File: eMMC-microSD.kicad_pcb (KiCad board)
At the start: 4 copper layers, 15 x 17.6 mm, 45 parts, among them J1 Micro_SD_Card, J2 Micro_SD_Card, J3 Micro_SD_Card, J4 Micro_SD_Card, J5 Micro_SD_Card, U1 eMMC_5.1_BGA153, U2 eMMC_5.1_BGA153, U3 eMMC_5.1_BGA153, U4 eMMC_5.1_BGA153, U5 eMMC_5.1_BGA153

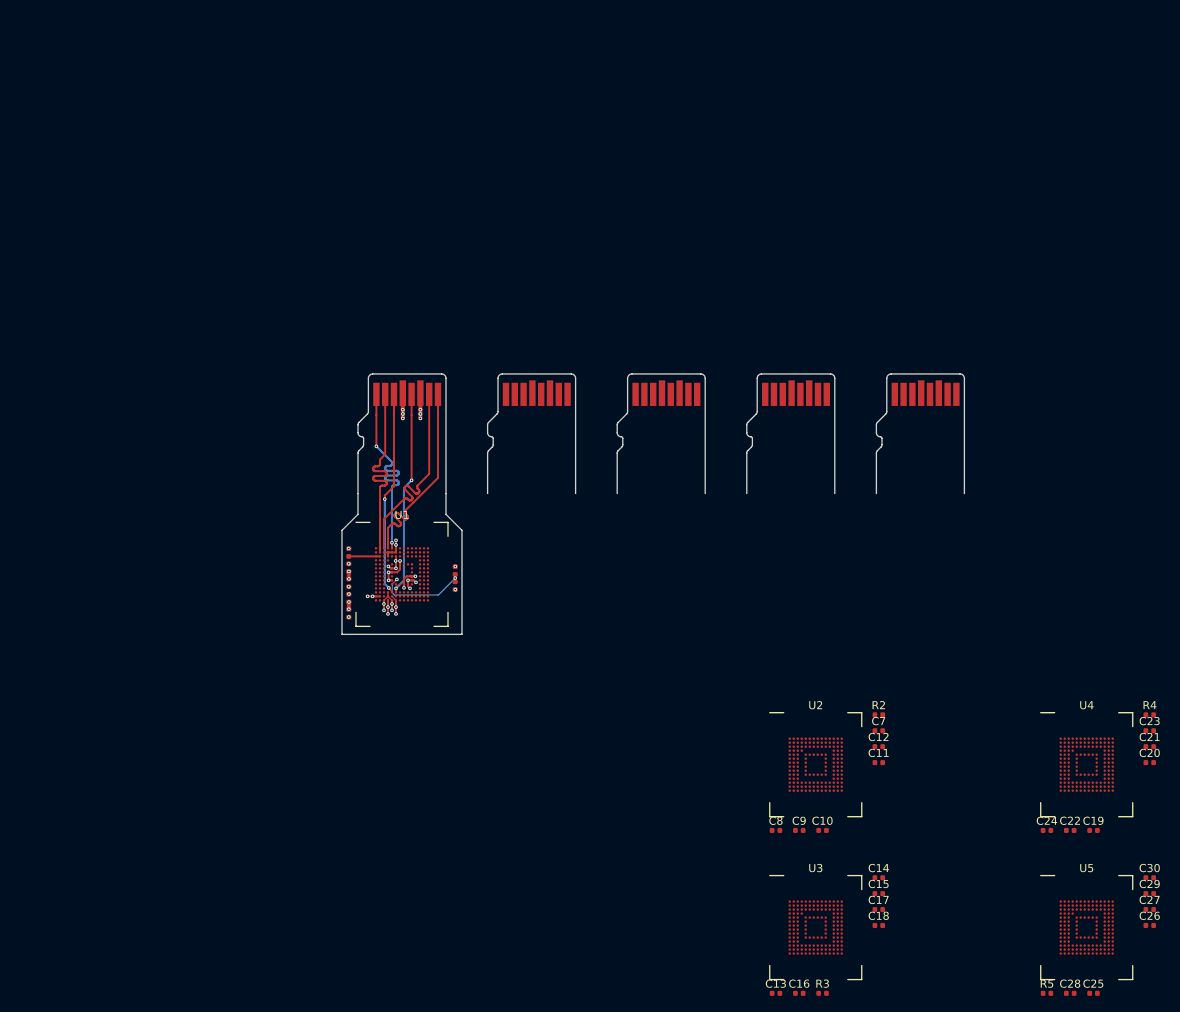
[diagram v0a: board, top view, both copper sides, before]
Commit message: Panelize
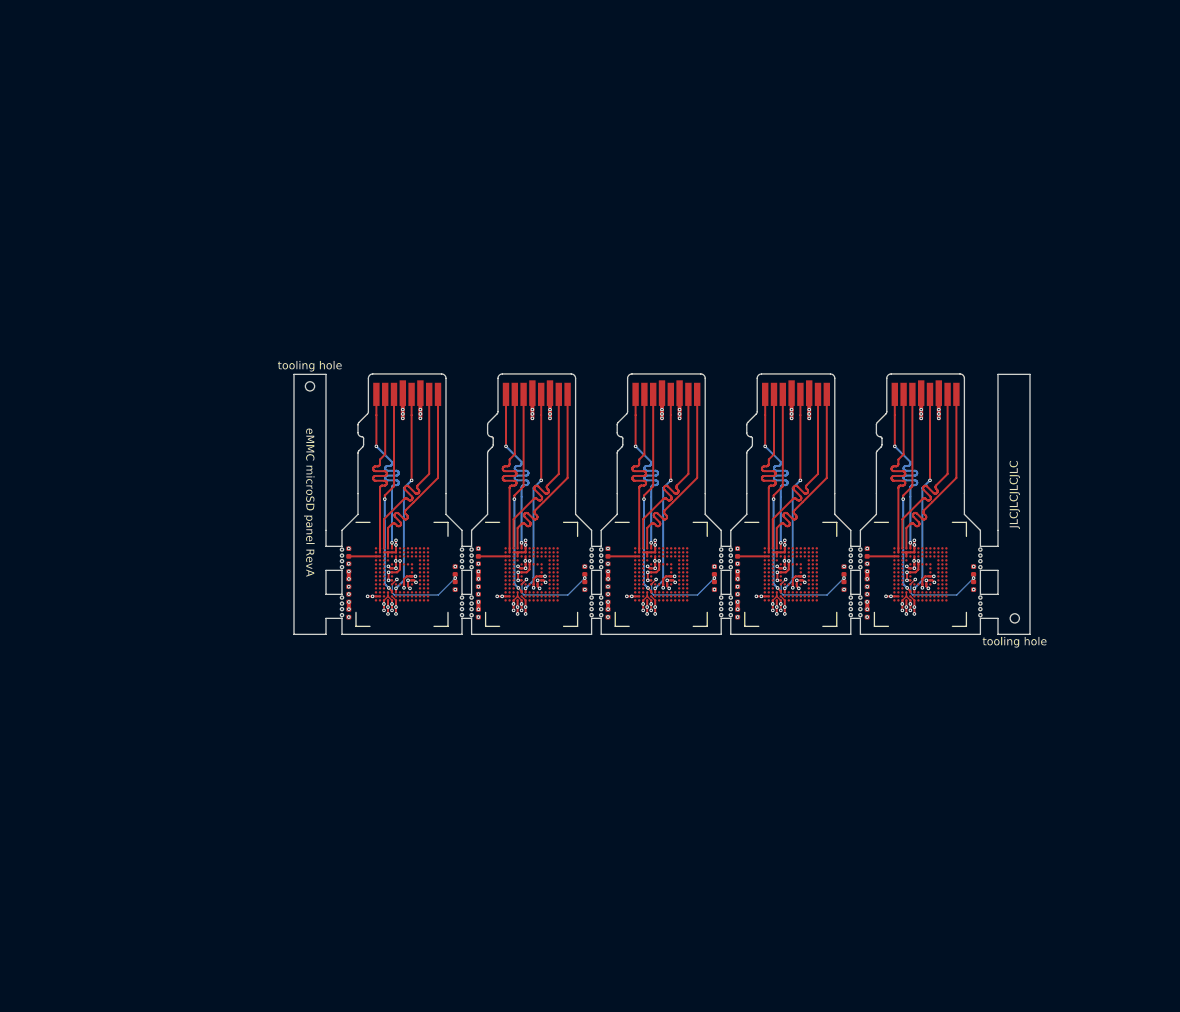
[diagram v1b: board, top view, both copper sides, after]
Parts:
- added REF**: ToolingHole_JLCSMT, ToolingHole:ToolingHole_JLCSMT, F.Cu at (171.1, 143.0)
- added REF**: Perforation_0.4mm, Perforation:Perforation_0.4mm, F.Cu at (166.8, 141.8)
- added REF**: Perforation_0.4mm, Perforation:Perforation_0.4mm, F.Cu at (87.0, 141.8)
- added REF**: Perforation_0.4mm, Perforation:Perforation_0.4mm, F.Cu at (87.0, 135.2)
- added REF**: Perforation_0.4mm, Perforation:Perforation_0.4mm, F.Cu at (87.0, 141.2)
- added REF**: Perforation_0.4mm, Perforation:Perforation_0.4mm, F.Cu at (87.0, 135.8)
- added REF**: Perforation_0.4mm, Perforation:Perforation_0.4mm, F.Cu at (87.0, 142.6)
- added REF**: Perforation_0.4mm, Perforation:Perforation_0.4mm, F.Cu at (87.0, 140.4)
- added REF**: Perforation_0.4mm, Perforation:Perforation_0.4mm, F.Cu at (87.0, 136.6)
- added REF**: Perforation_0.4mm, Perforation:Perforation_0.4mm, F.Cu at (87.0, 134.4)
- added REF**: Perforation_0.4mm, Perforation:Perforation_0.4mm, F.Cu at (151.8, 141.8)
- added REF**: ToolingHole_JLCSMT, ToolingHole:ToolingHole_JLCSMT, F.Cu at (83.0, 114.0)
- added REF**: Perforation_0.4mm, Perforation:Perforation_0.4mm, F.Cu at (150.6, 141.2)
- added REF**: Perforation_0.4mm, Perforation:Perforation_0.4mm, F.Cu at (150.6, 141.8)
- added REF**: Perforation_0.4mm, Perforation:Perforation_0.4mm, F.Cu at (150.6, 134.4)
- added REF**: Perforation_0.4mm, Perforation:Perforation_0.4mm, F.Cu at (150.6, 140.4)
- added REF**: Perforation_0.4mm, Perforation:Perforation_0.4mm, F.Cu at (151.8, 135.2)
- added REF**: Perforation_0.4mm, Perforation:Perforation_0.4mm, F.Cu at (151.8, 141.2)
- added REF**: Perforation_0.4mm, Perforation:Perforation_0.4mm, F.Cu at (151.8, 135.8)
- added REF**: Perforation_0.4mm, Perforation:Perforation_0.4mm, F.Cu at (151.8, 142.6)
- added REF**: Perforation_0.4mm, Perforation:Perforation_0.4mm, F.Cu at (151.8, 140.4)
- added REF**: Perforation_0.4mm, Perforation:Perforation_0.4mm, F.Cu at (151.8, 136.6)
- added REF**: Perforation_0.4mm, Perforation:Perforation_0.4mm, F.Cu at (166.8, 134.4)
- added REF**: Perforation_0.4mm, Perforation:Perforation_0.4mm, F.Cu at (151.8, 134.4)
- added REF**: Perforation_0.4mm, Perforation:Perforation_0.4mm, F.Cu at (150.6, 136.6)
- added REF**: Perforation_0.4mm, Perforation:Perforation_0.4mm, F.Cu at (150.6, 142.6)
- added REF**: Perforation_0.4mm, Perforation:Perforation_0.4mm, F.Cu at (150.6, 135.2)
- added REF**: Perforation_0.4mm, Perforation:Perforation_0.4mm, F.Cu at (150.6, 135.8)
- added REF**: Perforation_0.4mm, Perforation:Perforation_0.4mm, F.Cu at (135.6, 141.8)
- added REF**: Perforation_0.4mm, Perforation:Perforation_0.4mm, F.Cu at (134.4, 141.2)
- added REF**: Perforation_0.4mm, Perforation:Perforation_0.4mm, F.Cu at (134.4, 141.8)
- added REF**: Perforation_0.4mm, Perforation:Perforation_0.4mm, F.Cu at (134.4, 134.4)
- added REF**: Perforation_0.4mm, Perforation:Perforation_0.4mm, F.Cu at (134.4, 140.4)
- added REF**: Perforation_0.4mm, Perforation:Perforation_0.4mm, F.Cu at (166.8, 142.6)
- added REF**: Perforation_0.4mm, Perforation:Perforation_0.4mm, F.Cu at (135.6, 135.2)
- added REF**: Perforation_0.4mm, Perforation:Perforation_0.4mm, F.Cu at (135.6, 141.2)
- added REF**: Perforation_0.4mm, Perforation:Perforation_0.4mm, F.Cu at (135.6, 135.8)
- added REF**: Perforation_0.4mm, Perforation:Perforation_0.4mm, F.Cu at (135.6, 142.6)
- added REF**: Perforation_0.4mm, Perforation:Perforation_0.4mm, F.Cu at (135.6, 140.4)
- added REF**: Perforation_0.4mm, Perforation:Perforation_0.4mm, F.Cu at (135.6, 136.6)
- added REF**: Perforation_0.4mm, Perforation:Perforation_0.4mm, F.Cu at (135.6, 134.4)
- added REF**: Perforation_0.4mm, Perforation:Perforation_0.4mm, F.Cu at (134.4, 136.6)
- added REF**: Perforation_0.4mm, Perforation:Perforation_0.4mm, F.Cu at (134.4, 142.6)
- added REF**: Perforation_0.4mm, Perforation:Perforation_0.4mm, F.Cu at (134.4, 135.2)
- added REF**: Perforation_0.4mm, Perforation:Perforation_0.4mm, F.Cu at (166.8, 141.2)
- added REF**: Perforation_0.4mm, Perforation:Perforation_0.4mm, F.Cu at (134.4, 135.8)
- added REF**: Perforation_0.4mm, Perforation:Perforation_0.4mm, F.Cu at (119.4, 141.8)
- added REF**: Perforation_0.4mm, Perforation:Perforation_0.4mm, F.Cu at (118.2, 141.2)
- added REF**: Perforation_0.4mm, Perforation:Perforation_0.4mm, F.Cu at (118.2, 141.8)
- added REF**: Perforation_0.4mm, Perforation:Perforation_0.4mm, F.Cu at (118.2, 134.4)
- added REF**: Perforation_0.4mm, Perforation:Perforation_0.4mm, F.Cu at (118.2, 140.4)
- added REF**: Perforation_0.4mm, Perforation:Perforation_0.4mm, F.Cu at (119.4, 135.2)
- added REF**: Perforation_0.4mm, Perforation:Perforation_0.4mm, F.Cu at (119.4, 141.2)
- added REF**: Perforation_0.4mm, Perforation:Perforation_0.4mm, F.Cu at (119.4, 135.8)
- added REF**: Perforation_0.4mm, Perforation:Perforation_0.4mm, F.Cu at (119.4, 142.6)
- added REF**: Perforation_0.4mm, Perforation:Perforation_0.4mm, F.Cu at (166.8, 135.2)
- added REF**: Perforation_0.4mm, Perforation:Perforation_0.4mm, F.Cu at (119.4, 140.4)
- added REF**: Perforation_0.4mm, Perforation:Perforation_0.4mm, F.Cu at (119.4, 136.6)
- added REF**: Perforation_0.4mm, Perforation:Perforation_0.4mm, F.Cu at (119.4, 134.4)
- added REF**: Perforation_0.4mm, Perforation:Perforation_0.4mm, F.Cu at (118.2, 136.6)
- added REF**: Perforation_0.4mm, Perforation:Perforation_0.4mm, F.Cu at (118.2, 142.6)
- added REF**: Perforation_0.4mm, Perforation:Perforation_0.4mm, F.Cu at (118.2, 135.2)
- added REF**: Perforation_0.4mm, Perforation:Perforation_0.4mm, F.Cu at (118.2, 135.8)
- added REF**: Perforation_0.4mm, Perforation:Perforation_0.4mm, F.Cu at (103.2, 140.4)
- added REF**: Perforation_0.4mm, Perforation:Perforation_0.4mm, F.Cu at (103.2, 142.6)
- added REF**: Perforation_0.4mm, Perforation:Perforation_0.4mm, F.Cu at (103.2, 141.2)
- added REF**: Perforation_0.4mm, Perforation:Perforation_0.4mm, F.Cu at (166.8, 135.8)
- added REF**: Perforation_0.4mm, Perforation:Perforation_0.4mm, F.Cu at (103.2, 141.8)
- added REF**: Perforation_0.4mm, Perforation:Perforation_0.4mm, F.Cu at (102.0, 140.4)
- added REF**: Perforation_0.4mm, Perforation:Perforation_0.4mm, F.Cu at (102.0, 142.6)
- added REF**: Perforation_0.4mm, Perforation:Perforation_0.4mm, F.Cu at (102.0, 141.2)
- added REF**: Perforation_0.4mm, Perforation:Perforation_0.4mm, F.Cu at (102.0, 141.8)
- added REF**: Perforation_0.4mm, Perforation:Perforation_0.4mm, F.Cu at (103.2, 134.4)
- added REF**: Perforation_0.4mm, Perforation:Perforation_0.4mm, F.Cu at (103.2, 136.6)
- added REF**: Perforation_0.4mm, Perforation:Perforation_0.4mm, F.Cu at (103.2, 135.2)
- added REF**: Perforation_0.4mm, Perforation:Perforation_0.4mm, F.Cu at (103.2, 135.8)
- added REF**: Perforation_0.4mm, Perforation:Perforation_0.4mm, F.Cu at (102.0, 135.2)
- added REF**: Perforation_0.4mm, Perforation:Perforation_0.4mm, F.Cu at (166.8, 136.6)
- added REF**: Perforation_0.4mm, Perforation:Perforation_0.4mm, F.Cu at (102.0, 135.8)
- added REF**: Perforation_0.4mm, Perforation:Perforation_0.4mm, F.Cu at (102.0, 136.6)
- added REF**: Perforation_0.4mm, Perforation:Perforation_0.4mm, F.Cu at (102.0, 134.4)
- added REF**: Perforation_0.4mm, Perforation:Perforation_0.4mm, F.Cu at (166.8, 140.4)
- moved C26 58.5 mm to (152.7, 134.8), turned to 90 degrees
- moved C20 57.8 mm to (136.4, 134.8), turned to 90 degrees
- moved C28 57.2 mm to (152.7, 138.6), turned to 270 degrees
- moved C16 56.6 mm to (120.2, 138.6), turned to 270 degrees
- moved C18 56.1 mm to (120.2, 136.7), turned to 90 degrees
- moved C25 54.9 mm to (165.9, 137.0), turned to 270 degrees
- moved C12 54.8 mm to (104.0, 136.7), turned to 90 degrees
- moved C21 54.8 mm to (136.4, 140.5), turned to 90 degrees
- moved C23 53.6 mm to (136.4, 142.4), turned to 270 degrees
- moved C11 53.4 mm to (104.0, 142.4), turned to 270 degrees
- moved C13 53.4 mm to (133.6, 137.0), turned to 270 degrees
- moved C10 53.0 mm to (104.0, 138.6), turned to 270 degrees
- moved C14 52.9 mm to (120.2, 134.8), turned to 90 degrees
- moved R3 52.7 mm to (133.6, 138.9), turned to 90 degrees
- moved C27 52.6 mm to (152.7, 140.5), turned to 90 degrees
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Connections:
- U1 pad A2: (no net) -> /Adapter 1/DAT3
- U2 pad A2: (no net) -> /Adapter 2/DAT3
- U3 pad A2: (no net) -> /Adapter 3/DAT3
- U4 pad A2: (no net) -> /Adapter 4/DAT3
- U5 pad A2: (no net) -> /Adapter 5/DAT3
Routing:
- net GND: track 19.2 -> 96.1 mm, vias 22 -> 110
- net VCC: track 14.1 -> 70.4 mm, vias 18 -> 90
- net /Adapter 3/DAT3: track 0.00 -> 25.6 mm
- net /Adapter 4/DAT3: track 0.00 -> 25.6 mm
- net /Adapter 2/DAT3: track 0.00 -> 25.6 mm
- net /Sheet5F2931E6/DAT3: track 25.6 -> 0.00 mm
- net /Adapter 1/DAT3: track 0.00 -> 25.6 mm
- net /Adapter 5/DAT3: track 0.00 -> 25.6 mm
- net /Adapter 5/DAT2: track 0.00 -> 25.6 mm, vias 0 -> 2
- net /Adapter 4/DAT2: track 0.00 -> 25.6 mm, vias 0 -> 2
- net /Adapter 2/DAT2: track 0.00 -> 25.6 mm, vias 0 -> 2
- net /Adapter 3/DAT2: track 0.00 -> 25.6 mm, vias 0 -> 2
- net /Adapter 2/DAT1: track 0.00 -> 25.6 mm
- net /Adapter 5/DAT1: track 0.00 -> 25.6 mm
- net /Adapter 4/DAT1: track 0.00 -> 25.6 mm
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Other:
- board size 15 x 17.6 mm -> 92 x 32.5 mm
- board text added: "JLCJLCJLCJLC"
- board text added: "eMMC micro SD Rev A Tobias Schramm 2020"
- board text added: "eMMC microSD panel RevA"

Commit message: Redo termination and layout of first module
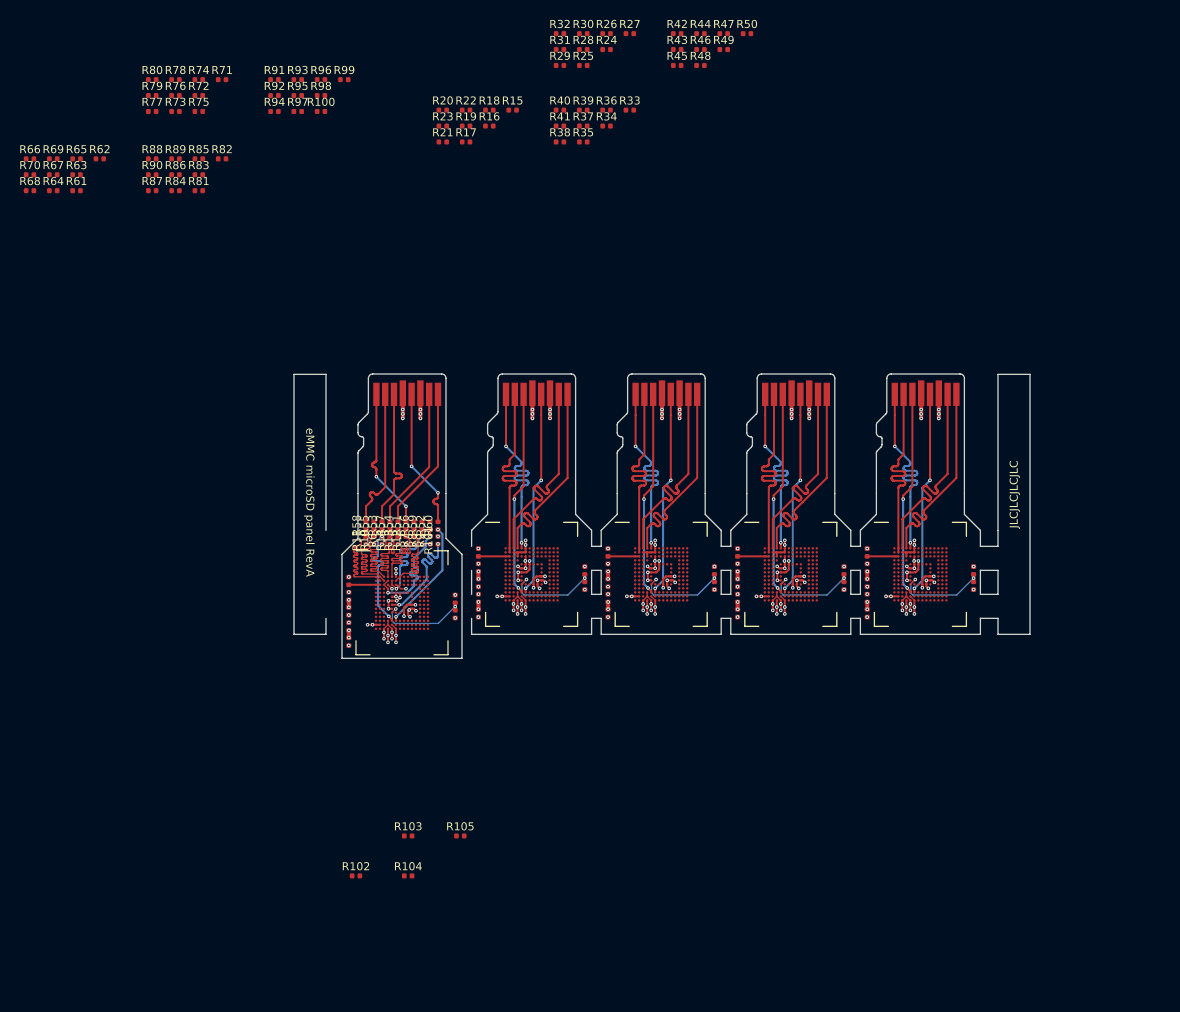
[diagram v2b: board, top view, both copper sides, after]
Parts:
- removed REF** (x2): ToolingHole_JLCSMT, ToolingHole:ToolingHole_JLCSMT
- removed REF** (x80): Perforation_0.4mm, Perforation:Perforation_0.4mm
- added R10: 10kR, Resistor_SMD:R_0402_1005Metric, F.Cu at (91.0, 133.2)
- added R100: 33R, Resistor_SMD:R_0402_1005Metric, F.Cu at (84.4, 79.6)
- added R101: 10kR, Resistor_SMD:R_0402_1005Metric, F.Cu at (99.0, 133.2)
- added R102: 10kR, Resistor_SMD:R_0402_1005Metric, F.Cu at (88.8, 175.2)
- added R103: 10kR, Resistor_SMD:R_0402_1005Metric, F.Cu at (95.3, 170.2)
- added R104: 10kR, Resistor_SMD:R_0402_1005Metric, F.Cu at (95.3, 175.2)
- added R105: 10kR, Resistor_SMD:R_0402_1005Metric, F.Cu at (101.8, 170.2)
- added R11: 10kR, Resistor_SMD:R_0402_1005Metric, F.Cu at (90.0, 133.2)
- added R12: 10kR, Resistor_SMD:R_0402_1005Metric, F.Cu at (95.0, 133.2)
- added R13: 10kR, Resistor_SMD:R_0402_1005Metric, F.Cu at (94.0, 133.2)
- added R14: 10kR, Resistor_SMD:R_0402_1005Metric, F.Cu at (93.0, 133.2)
- added R15: 10kR, Resistor_SMD:R_0402_1005Metric, F.Cu at (108.3, 79.5)
- added R16: 10kR, Resistor_SMD:R_0402_1005Metric, F.Cu at (105.4, 81.5)
- added R17: 10kR, Resistor_SMD:R_0402_1005Metric, F.Cu at (102.5, 83.5)
- added R18: 10kR, Resistor_SMD:R_0402_1005Metric, F.Cu at (105.4, 79.5)
- added R19: 10kR, Resistor_SMD:R_0402_1005Metric, F.Cu at (102.5, 81.5)
- added R20: 10kR, Resistor_SMD:R_0402_1005Metric, F.Cu at (99.6, 79.5)
- added R21: 10kR, Resistor_SMD:R_0402_1005Metric, F.Cu at (99.6, 83.5)
- added R22: 10kR, Resistor_SMD:R_0402_1005Metric, F.Cu at (102.5, 79.5)
- added R23: 10kR, Resistor_SMD:R_0402_1005Metric, F.Cu at (99.6, 81.5)
- added R24: 10kR, Resistor_SMD:R_0402_1005Metric, F.Cu at (120.1, 71.9)
- added R25: 10kR, Resistor_SMD:R_0402_1005Metric, F.Cu at (117.2, 73.9)
- added R26: 10kR, Resistor_SMD:R_0402_1005Metric, F.Cu at (120.1, 69.9)
- added R27: 10kR, Resistor_SMD:R_0402_1005Metric, F.Cu at (123.0, 69.9)
- added R28: 10kR, Resistor_SMD:R_0402_1005Metric, F.Cu at (117.2, 71.9)
- added R29: 10kR, Resistor_SMD:R_0402_1005Metric, F.Cu at (114.2, 73.9)
- added R30: 10kR, Resistor_SMD:R_0402_1005Metric, F.Cu at (117.2, 69.9)
- added R31: 10kR, Resistor_SMD:R_0402_1005Metric, F.Cu at (114.2, 71.9)
- added R32: 10kR, Resistor_SMD:R_0402_1005Metric, F.Cu at (114.2, 69.9)
- added R33: 10kR, Resistor_SMD:R_0402_1005Metric, F.Cu at (123.0, 79.5)
- added R34: 10kR, Resistor_SMD:R_0402_1005Metric, F.Cu at (120.1, 81.5)
- added R35: 10kR, Resistor_SMD:R_0402_1005Metric, F.Cu at (117.2, 83.5)
- added R36: 10kR, Resistor_SMD:R_0402_1005Metric, F.Cu at (120.1, 79.5)
- added R37: 10kR, Resistor_SMD:R_0402_1005Metric, F.Cu at (117.2, 81.5)
- added R38: 10kR, Resistor_SMD:R_0402_1005Metric, F.Cu at (114.2, 83.5)
- added R39: 10kR, Resistor_SMD:R_0402_1005Metric, F.Cu at (117.2, 79.5)
- added R40: 10kR, Resistor_SMD:R_0402_1005Metric, F.Cu at (114.2, 79.5)
- added R41: 10kR, Resistor_SMD:R_0402_1005Metric, F.Cu at (114.2, 81.5)
- added R42: 10kR, Resistor_SMD:R_0402_1005Metric, F.Cu at (128.9, 69.9)
- added R43: 10kR, Resistor_SMD:R_0402_1005Metric, F.Cu at (128.9, 71.9)
- added R44: 10kR, Resistor_SMD:R_0402_1005Metric, F.Cu at (131.8, 69.9)
- added R45: 10kR, Resistor_SMD:R_0402_1005Metric, F.Cu at (128.9, 73.9)
- added R46: 10kR, Resistor_SMD:R_0402_1005Metric, F.Cu at (131.8, 71.9)
- added R47: 10kR, Resistor_SMD:R_0402_1005Metric, F.Cu at (134.7, 69.9)
- added R48: 10kR, Resistor_SMD:R_0402_1005Metric, F.Cu at (131.8, 73.9)
- added R49: 10kR, Resistor_SMD:R_0402_1005Metric, F.Cu at (134.7, 71.9)
- added R50: 10kR, Resistor_SMD:R_0402_1005Metric, F.Cu at (137.6, 69.9)
- added R51: 33R, Resistor_SMD:R_0402_1005Metric, F.Cu at (95.0, 131.4)
- added R52: 33R, Resistor_SMD:R_0402_1005Metric, F.Cu at (98.0, 131.4)
- added R53: 33R, Resistor_SMD:R_0402_1005Metric, F.Cu at (92.0, 131.4)
- added R54: 33R, Resistor_SMD:R_0402_1005Metric, F.Cu at (94.0, 131.4)
- added R55: 33R, Resistor_SMD:R_0402_1005Metric, F.Cu at (91.0, 131.4)
- added R56: 33R, Resistor_SMD:R_0402_1005Metric, F.Cu at (96.0, 131.4)
- added R57: 33R, Resistor_SMD:R_0402_1005Metric, F.Cu at (93.0, 131.4)
- added R58: 33R, Resistor_SMD:R_0402_1005Metric, F.Cu at (90.0, 131.4)
- added R59: 33R, Resistor_SMD:R_0402_1005Metric, F.Cu at (97.0, 131.4)
- added R6: 10kR, Resistor_SMD:R_0402_1005Metric, F.Cu at (92.0, 133.2)
- added R60: 33R, Resistor_SMD:R_0402_1005Metric, F.Cu at (99.0, 131.4)
- added R61: 33R, Resistor_SMD:R_0402_1005Metric, F.Cu at (53.8, 89.5)
- added R62: 33R, Resistor_SMD:R_0402_1005Metric, F.Cu at (56.7, 85.6)
- added R63: 33R, Resistor_SMD:R_0402_1005Metric, F.Cu at (53.8, 87.5)
- added R64: 33R, Resistor_SMD:R_0402_1005Metric, F.Cu at (50.9, 89.5)
- added R65: 33R, Resistor_SMD:R_0402_1005Metric, F.Cu at (53.8, 85.6)
- added R66: 33R, Resistor_SMD:R_0402_1005Metric, F.Cu at (48.0, 85.6)
- added R67: 33R, Resistor_SMD:R_0402_1005Metric, F.Cu at (50.9, 87.5)
- added R68: 33R, Resistor_SMD:R_0402_1005Metric, F.Cu at (48.0, 89.5)
- added R69: 33R, Resistor_SMD:R_0402_1005Metric, F.Cu at (50.9, 85.6)
- added R7: 10kR, Resistor_SMD:R_0402_1005Metric, F.Cu at (96.0, 133.2)
- added R70: 33R, Resistor_SMD:R_0402_1005Metric, F.Cu at (48.0, 87.5)
- added R71: 33R, Resistor_SMD:R_0402_1005Metric, F.Cu at (72.0, 75.7)
- added R72: 33R, Resistor_SMD:R_0402_1005Metric, F.Cu at (69.1, 77.7)
- added R73: 33R, Resistor_SMD:R_0402_1005Metric, F.Cu at (66.2, 79.6)
- added R74: 33R, Resistor_SMD:R_0402_1005Metric, F.Cu at (69.1, 75.7)
- added R75: 33R, Resistor_SMD:R_0402_1005Metric, F.Cu at (69.1, 79.6)
- added R76: 33R, Resistor_SMD:R_0402_1005Metric, F.Cu at (66.2, 77.7)
- added R77: 33R, Resistor_SMD:R_0402_1005Metric, F.Cu at (63.3, 79.6)
- added R78: 33R, Resistor_SMD:R_0402_1005Metric, F.Cu at (66.2, 75.7)
- added R79: 33R, Resistor_SMD:R_0402_1005Metric, F.Cu at (63.3, 77.7)
- added R8: 10kR, Resistor_SMD:R_0402_1005Metric, F.Cu at (97.0, 133.2)
- added R80: 33R, Resistor_SMD:R_0402_1005Metric, F.Cu at (63.3, 75.7)
- added R81: 33R, Resistor_SMD:R_0402_1005Metric, F.Cu at (69.1, 89.5)
- added R82: 33R, Resistor_SMD:R_0402_1005Metric, F.Cu at (72.0, 85.6)
- added R83: 33R, Resistor_SMD:R_0402_1005Metric, F.Cu at (69.1, 87.5)
- added R84: 33R, Resistor_SMD:R_0402_1005Metric, F.Cu at (66.2, 89.5)
- added R85: 33R, Resistor_SMD:R_0402_1005Metric, F.Cu at (69.1, 85.6)
- added R86: 33R, Resistor_SMD:R_0402_1005Metric, F.Cu at (66.2, 87.5)
- added R87: 33R, Resistor_SMD:R_0402_1005Metric, F.Cu at (63.3, 89.5)
- added R88: 33R, Resistor_SMD:R_0402_1005Metric, F.Cu at (63.3, 85.6)
- added R89: 33R, Resistor_SMD:R_0402_1005Metric, F.Cu at (66.2, 85.6)
- added R9: 10kR, Resistor_SMD:R_0402_1005Metric, F.Cu at (98.0, 133.2)
- added R90: 33R, Resistor_SMD:R_0402_1005Metric, F.Cu at (63.3, 87.5)
- added R91: 33R, Resistor_SMD:R_0402_1005Metric, F.Cu at (78.6, 75.7)
- added R92: 33R, Resistor_SMD:R_0402_1005Metric, F.Cu at (78.6, 77.7)
- added R93: 33R, Resistor_SMD:R_0402_1005Metric, F.Cu at (81.5, 75.7)
- added R94: 33R, Resistor_SMD:R_0402_1005Metric, F.Cu at (78.6, 79.6)
- added R95: 33R, Resistor_SMD:R_0402_1005Metric, F.Cu at (81.5, 77.7)
- added R96: 33R, Resistor_SMD:R_0402_1005Metric, F.Cu at (84.4, 75.7)
- added R97: 33R, Resistor_SMD:R_0402_1005Metric, F.Cu at (81.5, 79.6)
- added R98: 33R, Resistor_SMD:R_0402_1005Metric, F.Cu at (84.4, 77.7)
- added R99: 33R, Resistor_SMD:R_0402_1005Metric, F.Cu at (87.3, 75.7)
- moved C4 3.55 mm to (87.8, 142.1)
- moved C6 3.55 mm to (87.8, 140.2)
- moved R1 3.55 mm to (101.2, 142.5)
- moved U1 3.55 mm to (94.5, 141.1)
- moved C1 3.55 mm to (101.2, 140.6)
- moved C2 3.55 mm to (87.8, 138.3)
- moved C3 3.55 mm to (87.8, 144.0)
- moved C5 3.55 mm to (87.8, 145.9)
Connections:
- U1 pad A1: (no net) -> /Adapter 1/D3
- U1 pad A2: /Adapter 1/DAT3 -> /Adapter 1/D4
- U1 pad A3: /Adapter 1/DAT0 -> Net-(R14-Pad2)
- U1 pad A4: /Adapter 1/DAT1 -> Net-(R13-Pad2)
- U1 pad A5: /Adapter 1/DAT2 -> Net-(R12-Pad2)
- U1 pad A7: (no net) -> /Adapter 1/D7
- U1 pad B2: /Adapter 1/DAT3 -> /Adapter 1/D3
- U1 pad B3: GND -> /Adapter 1/D4
- U1 pad B4: GND -> /Adapter 1/D5
- U1 pad B5: GND -> /Adapter 1/D6
- U1 pad B6: GND -> /Adapter 1/D7
- U1 pad C3: (no net) -> /Adapter 1/D5
- U1 pad C5: (no net) -> /Adapter 1/D6
- U1 pad D4: (no net) -> /Adapter 1/D5
- U1 pad M5: /Adapter 1/CMD -> Net-(R53-Pad1)
- U1 pad M6: /Adapter 1/CLK -> Net-(R60-Pad1)
- U2 pad A1: (no net) -> /Adapter 2/D3
- U2 pad A2: /Adapter 2/DAT3 -> /Adapter 2/D4
- U2 pad A3: /Adapter 2/DAT0 -> Net-(R23-Pad2)
- U2 pad A4: /Adapter 2/DAT1 -> Net-(R22-Pad2)
- U2 pad A5: /Adapter 2/DAT2 -> Net-(R21-Pad2)
- U2 pad A7: (no net) -> /Adapter 2/D7
- U2 pad B2: /Adapter 2/DAT3 -> /Adapter 2/D3
- U2 pad B3: GND -> /Adapter 2/D4
- U2 pad B4: GND -> /Adapter 2/D5
- U2 pad B5: GND -> /Adapter 2/D6
- U2 pad B6: GND -> /Adapter 2/D7
- U2 pad C3: (no net) -> /Adapter 2/D5
- U2 pad C5: (no net) -> /Adapter 2/D6
- U2 pad D4: (no net) -> /Adapter 2/D5
- U2 pad M5: /Adapter 2/CMD -> Net-(R15-Pad2)
- U2 pad M6: /Adapter 2/CLK -> Net-(R70-Pad1)
- U3 pad A1: (no net) -> /Adapter 3/D3
- U3 pad A2: /Adapter 3/DAT3 -> /Adapter 3/D4
- U3 pad A3: /Adapter 3/DAT0 -> Net-(R32-Pad2)
- U3 pad A4: /Adapter 3/DAT1 -> Net-(R31-Pad2)
- U3 pad A5: /Adapter 3/DAT2 -> Net-(R30-Pad2)
- U3 pad A7: (no net) -> /Adapter 3/D7
- U3 pad B2: /Adapter 3/DAT3 -> /Adapter 3/D3
- U3 pad B3: GND -> /Adapter 3/D4
- U3 pad B4: GND -> /Adapter 3/D5
- U3 pad B5: GND -> /Adapter 3/D6
- U3 pad B6: GND -> /Adapter 3/D7
- U3 pad C3: (no net) -> /Adapter 3/D5
- U3 pad C5: (no net) -> /Adapter 3/D6
- U3 pad D4: (no net) -> /Adapter 3/D5
- U3 pad M5: /Adapter 3/CMD -> Net-(R24-Pad2)
- U3 pad M6: /Adapter 3/CLK -> Net-(R80-Pad1)
- U4 pad A1: (no net) -> /Adapter 4/D3
- U4 pad A2: /Adapter 4/DAT3 -> /Adapter 4/D4
- U4 pad A3: /Adapter 4/DAT0 -> Net-(R41-Pad2)
- U4 pad A4: /Adapter 4/DAT1 -> Net-(R40-Pad2)
- U4 pad A5: /Adapter 4/DAT2 -> Net-(R39-Pad2)
- U4 pad A7: (no net) -> /Adapter 4/D7
- U4 pad B2: /Adapter 4/DAT3 -> /Adapter 4/D3
- U4 pad B3: GND -> /Adapter 4/D4
- U4 pad B4: GND -> /Adapter 4/D5
- U4 pad B5: GND -> /Adapter 4/D6
- U4 pad B6: GND -> /Adapter 4/D7
- U4 pad C3: (no net) -> /Adapter 4/D5
- U4 pad C5: (no net) -> /Adapter 4/D6
- U4 pad D4: (no net) -> /Adapter 4/D5
- U4 pad M5: /Adapter 4/CMD -> Net-(R33-Pad2)
- U4 pad M6: /Adapter 4/CLK -> Net-(R90-Pad1)
- U5 pad A1: (no net) -> /Adapter 5/D3
- U5 pad A2: /Adapter 5/DAT3 -> /Adapter 5/D4
- U5 pad A3: /Adapter 5/DAT0 -> Net-(R50-Pad2)
- U5 pad A4: /Adapter 5/DAT1 -> Net-(R49-Pad2)
- U5 pad A5: /Adapter 5/DAT2 -> Net-(R48-Pad2)
- U5 pad A7: (no net) -> /Adapter 5/D7
- U5 pad B2: /Adapter 5/DAT3 -> /Adapter 5/D3
- U5 pad B3: GND -> /Adapter 5/D4
- U5 pad B4: GND -> /Adapter 5/D5
- U5 pad B5: GND -> /Adapter 5/D6
- U5 pad B6: GND -> /Adapter 5/D7
- U5 pad C3: (no net) -> /Adapter 5/D5
- U5 pad C5: (no net) -> /Adapter 5/D6
- U5 pad D4: (no net) -> /Adapter 5/D5
- U5 pad M5: /Adapter 5/CMD -> Net-(R42-Pad2)
- U5 pad M6: /Adapter 5/CLK -> Net-(R100-Pad1)
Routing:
- net /Adapter 1/D5: track 0.00 -> 15.5 mm, vias 0 -> 2
- net /Adapter 1/D3: track 0.00 -> 14.4 mm
- net Net-(R14-Pad2): track 0.00 -> 14.1 mm
- net /Adapter 1/D6: track 0.00 -> 14.1 mm, vias 0 -> 2
- net Net-(R13-Pad2): track 0.00 -> 14.1 mm
- net Net-(R12-Pad2): track 0.00 -> 14.1 mm
- net /Adapter 1/D7: track 0.00 -> 14.1 mm
- net /Adapter 1/D4: track 0.00 -> 14.1 mm
- net Net-(R60-Pad1): track 0.00 -> 14.0 mm, vias 0 -> 2
- net Net-(R53-Pad1): track 0.00 -> 14.0 mm, vias 0 -> 2
- net Net-(R101-Pad1): track 0.00 -> 14.0 mm, vias 0 -> 2
- net /Adapter 1/DAT3: track 25.6 -> 18.0 mm
- net /Adapter 1/CMD: track 25.6 -> 18.0 mm, vias 2 -> 0
- net /Adapter 1/DAT1: track 25.6 -> 18.0 mm
- net /Adapter 1/DAT0: track 25.6 -> 17.9 mm
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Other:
- board size 92 x 32.5 mm -> 92 x 35.5 mm
